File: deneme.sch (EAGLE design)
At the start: 26 parts, among them Q2 BCX70SMD, Q3 BCX70SMD, Q4 BCX70SMD, Q5 BCX70SMD, Q6 BCX70SMD, Q7 BCX70SMD, Q8 BCX70SMD, Q9 BCX70SMD

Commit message: Ldr changed, curcuit was drawn  from the beginning
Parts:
- removed PH1, PH2: B1060_23, photo-elements:B1060_23
- added PH3, PH4: V1060_31, photo-elements:V1060_31
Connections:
- net GND: now also PH3.2, PH4.2; no longer PH1.2, PH2.2
- net N$4: now also PH3.1; no longer PH2.1
- net N$6: now also PH4.1; no longer PH1.1
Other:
- moved on the sheet: C1, C3, Q2, Q3, Q4, Q5, Q6, Q7, Q8, Q9, R1, R10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

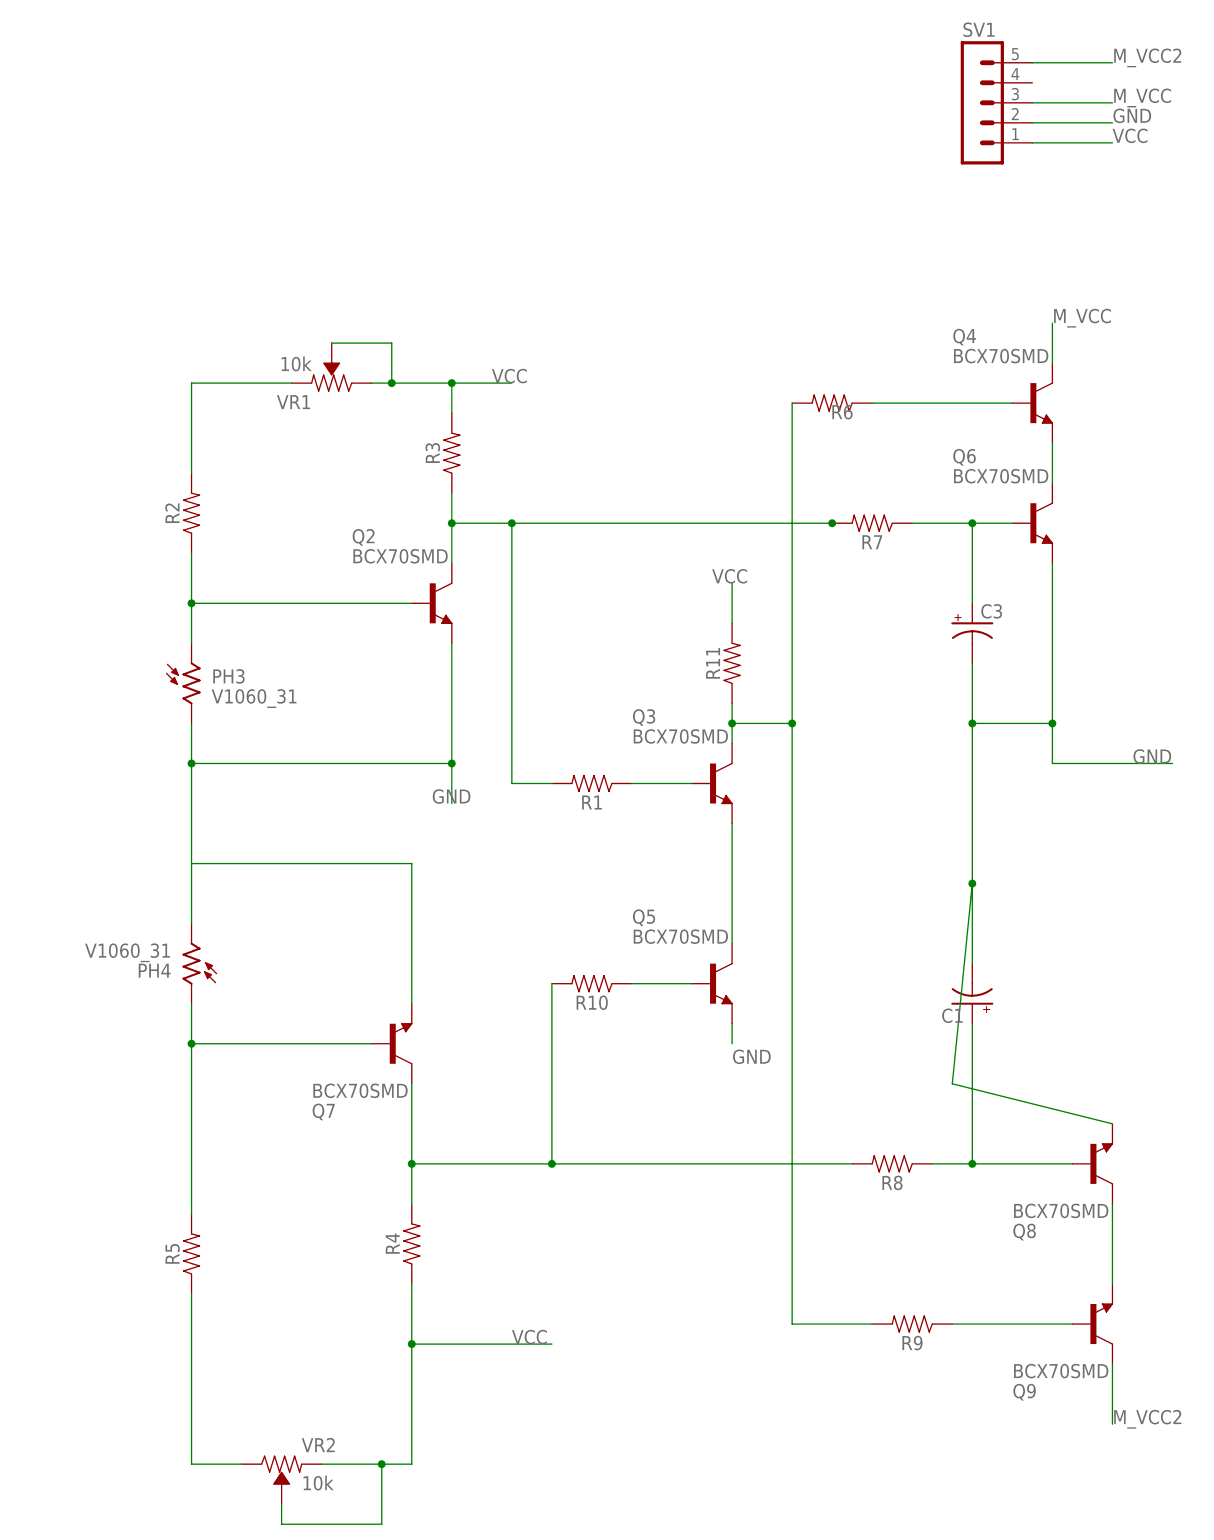
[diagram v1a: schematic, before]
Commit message: project finished
pot and ldr changed.  Shortcomings completed.
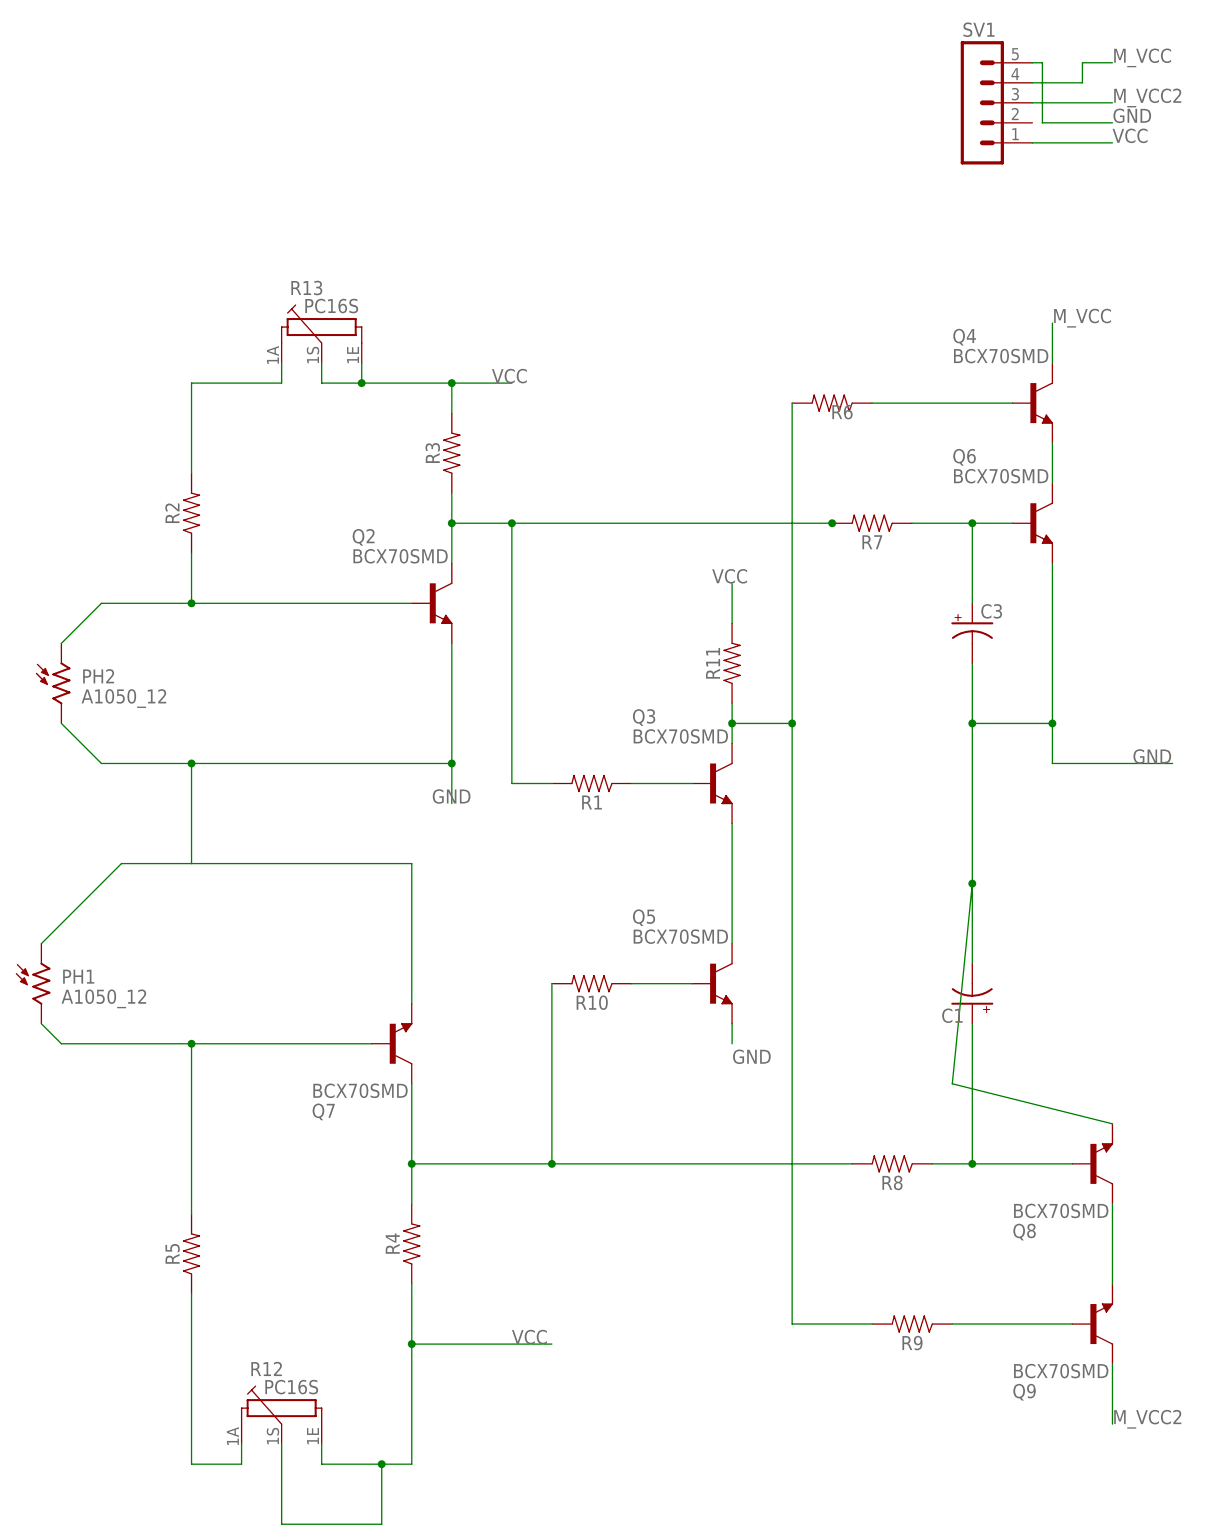
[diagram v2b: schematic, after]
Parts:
- removed PH3, PH4: V1060_31, photo-elements:V1060_31
- removed VR1, VR2: 10k, SparkFun-Resistors:TRIMPOT-PTH-10MM-KNOB-1/2W-10%
- added PH1, PH2: A1050_12, photo-elements:A1050_12
- added R12, R13: PC16S, piher:PC16S
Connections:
- net GND: now also PH1.1, PH2.2, SV1.5; no longer PH3.2, PH4.2, SV1.2
- net M_VCC: now also SV1.4; no longer SV1.3
- net M_VCC2: now also SV1.3; no longer SV1.5
- net N$1: now also R13.1A; no longer VR1.CCW
- net N$4: now also PH2.1; no longer PH3.1
- net N$6: now also PH1.2; no longer PH4.1
- net N$7: now also R12.1A; no longer VR2.CW
- net VCC: now also R12.1E, R12.1S, R13.1E, R13.1S; no longer VR1.CW, VR1.WIPER, VR2.CCW, VR2.WIPER
